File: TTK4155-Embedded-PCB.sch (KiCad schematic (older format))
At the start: 40 parts

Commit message: stated working on pcb
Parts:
- removed J?: AVR-JTAG-10, symbol Connector:AVR-JTAG-10
- removed U?: IDT7164S, Package_DIP:DIP-28_W7.62mm_Socket_LongPads, symbol ByggernCustom:IDT7164S
- added J1: AVR-JTAG-10, Connector_IDC:IDC-Header_2x05_P2.54mm_Vertical, symbol Connector:AVR-JTAG-10
- added U3: IDT7164S, Package_DIP:DIP-28_W7.62mm_Socket_LongPads, symbol ByggernCustom:IDT7164S
- U5: renamed from U?; footprint SN74ALS573CN:DIP254P762X508-20 -> Package_DIP:DIP-20_W7.62mm_Socket_LongPads
- gave numbers to parts that had none: 37
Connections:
- net +5V: now also J1.4 (VREF), J1.7 (VCC), U3.28 (Vcc)
- net A0: now also U3.19 (I/O_7)
- net A1: now also U3.18 (I/O_6)
- net A10: now also U3.21 (A10)
- net A11: now also U3.23 (A11)
- net A2: now also U3.17 (I/O_5)
- net A3: now also U3.16 (I/O_4)
- net A4: now also U3.15 (I/O_3)
- net A5: now also U3.11 (I/O_0)
- net A6: now also U3.12 (I/O_1)
- net A7: now also U3.13 (I/O_2)
- net A8: now also U3.25 (A8)
- net A9: now also U3.24 (A9)
- net CS_RAM: now also U3.26 (CS)
- net GND: now also J1.10 (GND), J1.2 (GND), U3.14 (GND), U3.2 (A12), U3.20 (~CS)
- net TCK: now also J1.1 (TCK)
- net TDI: now also J1.9 (TDI)
- net TDO: now also J1.3 (TDO)
- net TMS: now also J1.5 (TMS)
- net ~OE: now also U3.22 (~OE)
- net ~RESET: now also J1.6 (~SRST)
- net ~WE: now also U3.27 (~WE)
- net at U5.12 (8Q): now also U3.10 (A0)
- net at U5.13 (7Q): now also U3.9 (A1)
- net at U5.14 (6Q): now also U3.8 (A2)
- net at U5.15 (5Q): now also U3.7 (A3)
- net at U5.16 (4Q): now also U3.6 (A4)
- net at U5.17 (3Q): now also U3.5 (A5)
- net at U5.18 (2Q): now also U3.4 (A6)
- net at U5.19 (1Q): now also U3.3 (A7)

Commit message: Started tracing
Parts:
- removed J3: Conn_01x08_Male, Connector_PinHeader_2.00mm:PinHeader_1x08_P2.00mm_Vertical, symbol Connector:Conn_01x08_Male
- removed J5: Conn_01x02_Male, Connector_PinHeader_2.00mm:PinHeader_1x02_P2.00mm_Vertical, symbol Connector:Conn_01x02_Male
- added J3: Conn_01x10_Male, Connector_PinHeader_2.54mm:PinHeader_1x10_P2.54mm_Vertical, symbol Connector:Conn_01x10_Male
- added J5, J6: Screw_Terminal_01x02, TerminalBlock_MetzConnect:TerminalBlock_MetzConnect_Type073_RT02602HBLU_1x02_P5.08mm_Horizontal, symbol Connector:Screw_Terminal_01x02
- added R6: 60R, Resistor_SMD:R_0805_2012Metric_Pad1.15x1.40mm_HandSolder, symbol Device:R
- J4: footprint Connector_PinHeader_2.00mm:PinHeader_1x04_P2.00mm_Vertical -> Connector_PinHeader_2.54mm:PinHeader_1x04_P2.54mm_Vertical
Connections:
- net A0: now also J3.1 (Pin_1)
- net A1: now also J3.2 (Pin_2)
- net A10: now also U3.24 (A9), U4.2 (I2); no longer U3.21 (A10), U4.3 (I3)
- net A11: now also U3.25 (A8), U4.1 (I1/CLK); no longer U3.23 (A11), U4.4 (I4)
- net A2: now also J3.3 (Pin_3)
- net A3: now also J3.4 (Pin_4)
- net A4: now also J3.5 (Pin_5)
- net A5: now also J3.6 (Pin_6)
- net A6: now also J3.7 (Pin_7)
- net A7: now also J3.8 (Pin_8)
- net A8: now also U3.21 (A10); no longer U3.25 (A8), U4.1 (I1/CLK)
- net A9: now also U3.23 (A11), U4.3 (I3); no longer U3.24 (A9), U4.2 (I2)
- net GND: now also J6.2 (Pin_2)
- net OLED_CMD: now also J3.10 (Pin_10)
- net OLED_DATA: now also J3.9 (Pin_9)
- net at U7.6 (CANL): now also J5.2 (Pin_2), R6.2
- net at U7.7 (CANH): now also J5.1 (Pin_1), R6.1
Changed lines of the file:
@@
 Text Label 3350 5300 0    50   ~ 0
 ~OE
-Wire Wire Line
-	4100 3700 4100 3900
-Wire Wire Line
-	4100 3900 4300 3900
-Wire Wire Line
-	4050 3800 4050 4000
-Wire Wire Line
-	4050 4000 4300 4000
-Wire Wire Line
-	4000 4100 4300 4100
-Wire Wire Line
-	3950 4200 4300 4200
-Wire Wire Line
-	3950 4000 3950 4200
 $Comp
 L power:GND #PWR0120
@@
 Wire Wire Line
 	5550 3100 5100 3100
-Wire Wire Line
-	3350 3700 4100 3700
-Wire Wire Line
-	3350 3800 4050 3800
-Wire Wire Line
-	3350 3900 4000 3900
-Wire Wire Line
-	3350 4000 3950 4000
 $Comp
 L Logic_Programmable:GAL16V8 U4
@@
 	1    0    0    -1
 $EndComp
-Wire Wire Line
-	4000 3900 4000 4100
+Text Label 5100 2900 0    50   ~ 0
+A8
+Text Label 5100 3000 0    50   ~ 0
+A9
+Text Label 5100 2800 0    50   ~ 0
+A10
 Text Label 5100 2700 0    50   ~ 0
-A8
-Text Label 5100 2800 0    50   ~ 0
-A9
-Text Label 5100 2900 0    50   ~ 0
-A10
-Text Label 5100 3000 0    50   ~ 0
 A11
 Text Label 3800 3700 0    50   ~ 0
@@
 Reset button
 Wire Notes Line
-	1850 1250 3250 1250
-Wire Notes Line
 	3250 1250 3250 500
 Text Notes 1900 1250 0    50   ~ 0
@@
 Wire Wire Line
 	10050 3200 10000 3200
-Text Label 3650 1900 0    50   ~ 0
-A0
-Text Label 3650 2000 0    50   ~ 0
-A1
-Text Label 3650 2100 0    50   ~ 0
-A2
-Text Label 3650 2200 0    50   ~ 0
-A3
-Text Label 3650 2300 0    50   ~ 0
-A4
-Text Label 3650 2400 0    50   ~ 0
-A5
-Text Label 3650 2500 0    50   ~ 0
-A6
-Text Label 3650 2600 0    50   ~ 0
-A7
 Text Label 10950 2700 0    50   ~ 0
 A0
@@
 F 0 "J4" H 9358 2981 50  0000 C CNN
 F 1 "Conn_01x04_Male" H 9358 2890 50  0000 C CNN
-F 2 "Connector_PinHeader_2.00mm:PinHeader_1x04_P2.00mm_Vertical" H 9250 2700 50  0001 C CNN
+F 2 "Connector_PinHeader_2.54mm:PinHeader_1x04_P2.54mm_Vertical" H 9250 2700 50  0001 C CNN
 F 3 "~" H 9250 2700 50  0001 C CNN
 	1    9250 2700
@@
 Text Notes 10150 3700 0    50   ~ 0
 ADC Converter
-$Comp
-L Connector:Conn_01x08_Male J3
-U 1 1 5DC60D2B
-P 9200 4250
-F 0 "J3" H 9308 4731 50  0000 C CNN
-F 1 "Conn_01x08_Male" H 9308 4640 50  0000 C CNN
-F 2 "Connector_PinHeader_2.00mm:PinHeader_1x08_P2.00mm_Vertical" H 9200 4250 50  0001 C CNN
-F 3 "~" H 9200 4250 50  0001 C CNN
-	1    9200 4250
-	1    0    0    -1
-$EndComp
-Wire Wire Line
-	9400 3950 9600 3950
-Wire Wire Line
-	9400 4050 9600 4050
-Wire Wire Line
-	9400 4150 9600 4150
-Wire Wire Line
-	9400 4250 9600 4250
-Wire Wire Line
-	9400 4350 9600 4350
-Wire Wire Line
-	9400 4450 9600 4450
-Wire Wire Line
-	9400 4550 9600 4550
-Wire Wire Line
-	9400 4650 9600 4650
-Text Label 9600 3950 0    50   ~ 0
+Wire Wire Line
+	9750 3950 9950 3950
+Wire Wire Line
+	9750 4050 9950 4050
+Wire Wire Line
+	9750 4150 9950 4150
+Wire Wire Line
+	9750 4250 9950 4250
+Wire Wire Line
+	9750 4350 9950 4350
+Wire Wire Line
+	9750 4450 9950 4450
+Wire Wire Line
+	9750 4550 9950 4550
+Wire Wire Line
+	9750 4650 9950 4650
+Text Label 9950 3950 0    50   ~ 0
 A0
-Text Label 9600 4050 0    50   ~ 0
+Text Label 9950 4050 0    50   ~ 0
 A1
-Text Label 9600 4150 0    50   ~ 0
+Text Label 9950 4150 0    50   ~ 0
 A2
-Text Label 9600 4250 0    50   ~ 0
+Text Label 9950 4250 0    50   ~ 0
 A3
-Text Label 9600 4350 0    50   ~ 0
+Text Label 9950 4350 0    50   ~ 0
 A4
-Text Label 9600 4450 0    50   ~ 0
+Text Label 9950 4450 0    50   ~ 0
 A5
-Text Label 9600 4550 0    50   ~ 0
+Text Label 9950 4550 0    50   ~ 0
 A6
-Text Label 9600 4650 0    50   ~ 0
+Text Label 9950 4650 0    50   ~ 0
 A7
-Text Notes 9200 4750 0    50   ~ 0
+Text Notes 10150 3950 0    50   ~ 0
 Memory bus to ExtOLED
-$Comp
-L Connector:Conn_01x02_Male J5
-U 1 1 5DCBC334
-P 10450 4050
-F 0 "J5" H 10422 3932 50  0000 R CNN
-F 1 "Conn_01x02_Male" H 10422 4023 50  0000 R CNN
-F 2 "Connector_PinHeader_2.00mm:PinHeader_1x02_P2.00mm_Vertical" H 10450 4050 50  0001 C CNN
-F 3 "~" H 10450 4050 50  0001 C CNN
-	1    10450 4050
-	-1   0    0    1
-$EndComp
 Wire Wire Line
 	5300 4100 5500 4100
@@
 Text Label 5500 4200 0    50   ~ 0
 OLED_DATA
-Text Label 10250 4050 2    50   ~ 0
+Text Label 9750 4850 0    50   ~ 0
 OLED_CMD
-Text Label 10250 3950 2    50   ~ 0
+Text Label 9750 4750 0    50   ~ 0
 OLED_DATA
 Wire Notes Line
-	8950 4800 11200 4800
-Wire Notes Line
-	8950 500  8950 4800
-Text Notes 10000 4250 0    50   ~ 0
+	8950 4950 11200 4950
+Text Notes 10250 4850 0    50   ~ 0
 Selects between data \nand cmd registert\n
 Wire Wire Line
@@
 	1    0    0    -1
 $EndComp
+$Comp
+L Connector:Conn_01x10_Male J3
+U 1 1 5DC3E321
+P 9550 4350
+F 0 "J3" H 9658 4931 50  0000 C CNN
+F 1 "Conn_01x10_Male" H 9658 4840 50  0000 C CNN
+F 2 "Connector_PinHeader_2.54mm:PinHeader_1x10_P2.54mm_Vertical" H 9550 4350 50  0001 C CNN
+F 3 "~" H 9550 4350 50  0001 C CNN
+	1    9550 4350
+	1    0    0    -1
+$EndComp
+Wire Notes Line
+	8950 500  8950 4950
+$Comp
+L Device:R R6
+U 1 1 5DC5E47D
+P 10900 5700
+F 0 "R6" H 10970 5746 50  0000 L CNN
+F 1 "60R" H 10970 5655 50  0000 L CNN
+F 2 "Resistor_SMD:R_0805_2012Metric_Pad1.15x1.40mm_HandSolder" V 10830 5700 50  0001 C CNN
+F 3 "~" H 10900 5700 50  0001 C CNN
+	1    10900 5700
+	1    0    0    -1
+$EndComp
+Wire Wire Line
+	10800 5800 10800 5850
+Wire Wire Line
+	10800 5850 10900 5850
+Wire Wire Line
+	10800 5600 10800 5550
+Wire Wire Line
+	10800 5550 10900 5550
+Wire Wire Line
+	3350 4000 3800 4000
+Wire Wire Line
+	3350 3900 3800 3900
+Wire Wire Line
+	3350 3800 3800 3800
+Wire Wire Line
+	3350 3700 3800 3700
+Text Label 4300 3900 2    50   ~ 0
+A11
+Text Label 4300 4000 2    50   ~ 0
+A10
+Text Label 4300 4100 2    50   ~ 0
+A9
+$Comp
+L Connector:Screw_Terminal_01x02 J5
+U 1 1 5DCCBD1E
+P 11100 6300
+F 0 "J5" V 11100 5950 50  0000 L CNN
+F 1 "Screw_Terminal_01x02" V 11250 5550 50  0000 L CNN
+F 2 "TerminalBlock_MetzConnect:TerminalBlock_MetzConnect_Type073_RT02602HBLU_1x02_P5.08mm_Horizontal" H 11100 6300 50  0001 C CNN
+F 3 "~" H 11100 6300 50  0001 C CNN
+	1    11100 6300
+	0    1    1    0
+$EndComp
+Wire Wire Line
+	10900 5850 11000 5850
+Wire Wire Line
+	11000 5850 11000 6100
+Connection ~ 10900 5850
+Wire Wire Line
+	11100 5850 11150 5850
+Wire Wire Line
+	11150 5850 11150 5550
+Wire Wire Line
+	11150 5550 10900 5550
+Wire Wire Line
+	11100 5850 11100 6100
+Connection ~ 10900 5550
+$Comp
+L Connector:Screw_Terminal_01x02 J6
+U 1 1 5DD11A7E
+P 3550 700
+F 0 "J6" V 3550 350 50  0000 L CNN
+F 1 "Screw_Terminal_01x02" V 3700 100 50  0000 L CNN
+F 2 "TerminalBlock_MetzConnect:TerminalBlock_MetzConnect_Type073_RT02602HBLU_1x02_P5.08mm_Horizontal" H 3550 700 50  0001 C CNN
+F 3 "~" H 3550 700 50  0001 C CNN
+	1    3550 700
+	0    -1   -1   0
+$EndComp
+Wire Wire Line
+	3550 900  3550 1000
+Wire Wire Line
+	3550 1000 3350 1000
+$Comp
+L power:GND #PWR0134
+U 1 1 5DD5A4AB
+P 3650 900
+F 0 "#PWR0134" H 3650 650 50  0001 C CNN
+F 1 "GND" H 3655 727 50  0000 C CNN
+F 2 "" H 3650 900 50  0001 C CNN
+F 3 "" H 3650 900 50  0001 C CNN
+	1    3650 900
+	1    0    0    -1
+$EndComp
+Wire Notes Line
+	3800 1250 3800 950
+Wire Notes Line
+	3800 950  4200 950
+Wire Notes Line
+	4200 950  4200 500
+Wire Notes Line
+	1850 1250 3800 1250
+Text Label 3650 2600 0    50   ~ 0
+A7
+Text Label 3650 2500 0    50   ~ 0
+A6
+Text Label 3650 2400 0    50   ~ 0
+A5
+Text Label 3650 2300 0    50   ~ 0
+A4
+Text Label 3650 2200 0    50   ~ 0
+A3
+Text Label 3650 2100 0    50   ~ 0
+A2
+Text Label 3650 2000 0    50   ~ 0
+A1
+Text Label 3650 1900 0    50   ~ 0
+A0
 $EndSCHEMATC

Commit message: Finished first revision of board
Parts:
- added J7: Conn_01x04_Male, Connector_PinHeader_2.54mm:PinHeader_1x04_P2.54mm_Vertical, symbol Connector:Conn_01x04_Male
- added J8: BannanaJack, TTK4155-Embedded-PCB:Banana_Jack_2Pin_15mm_spacing, symbol Connector_Generic:Conn_01x02
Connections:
- net +12V: now also J6.1 (Pin_1), J8.1 (Pin_1)
- net GND: now also J8.2 (Pin_2)
- net at U2.1 (PB0): now also J7.4 (Pin_4)
- net at U2.2 (PB1): now also J7.3 (Pin_3)
- net at U2.3 (PB2): now also J7.2 (Pin_2)
- net at U2.4 (PB3): now also J7.1 (Pin_1)
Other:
- moved on the sheet: J6
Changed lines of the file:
@@
 L Connector:Screw_Terminal_01x02 J6
 U 1 1 5DD11A7E
-P 3550 700
-F 0 "J6" V 3550 350 50  0000 L CNN
-F 1 "Screw_Terminal_01x02" V 3700 100 50  0000 L CNN
-F 2 "TerminalBlock_MetzConnect:TerminalBlock_MetzConnect_Type073_RT02602HBLU_1x02_P5.08mm_Horizontal" H 3550 700 50  0001 C CNN
-F 3 "~" H 3550 700 50  0001 C CNN
-	1    3550 700
-	0    -1   -1   0
+P 8550 800
+F 0 "J6" V 8650 700 50  0000 L CNN
+F 1 "Screw_Terminal_01x02" V 8750 200 50  0001 L CNN
+F 2 "TerminalBlock_MetzConnect:TerminalBlock_MetzConnect_Type073_RT02602HBLU_1x02_P5.08mm_Horizontal" H 8550 800 50  0001 C CNN
+F 3 "~" H 8550 800 50  0001 C CNN
+	1    8550 800
+	1    0    0    -1
 $EndComp
-Wire Wire Line
-	3550 900  3550 1000
-Wire Wire Line
-	3550 1000 3350 1000
 $Comp
 L power:GND #PWR0134
 U 1 1 5DD5A4AB
-P 3650 900
-F 0 "#PWR0134" H 3650 650 50  0001 C CNN
-F 1 "GND" H 3655 727 50  0000 C CNN
-F 2 "" H 3650 900 50  0001 C CNN
-F 3 "" H 3650 900 50  0001 C CNN
-	1    3650 900
+P 8350 900
+F 0 "#PWR0134" H 8350 650 50  0001 C CNN
+F 1 "GND" H 8355 727 50  0000 C CNN
+F 2 "" H 8350 900 50  0001 C CNN
+F 3 "" H 8350 900 50  0001 C CNN
+	1    8350 900
 	1    0    0    -1
 $EndComp
-Wire Notes Line
-	3800 1250 3800 950
-Wire Notes Line
-	3800 950  4200 950
-Wire Notes Line
-	4200 950  4200 500
-Wire Notes Line
-	1850 1250 3800 1250
 Text Label 3650 2600 0    50   ~ 0
 A7
@@
 Text Label 3650 1900 0    50   ~ 0
 A0
+$Comp
+L power:+12V #PWR0135
+U 1 1 5DDD0920
+P 8350 800
+F 0 "#PWR0135" H 8350 650 50  0001 C CNN
+F 1 "+12V" H 8365 973 50  0000 C CNN
+F 2 "" H 8350 800 50  0001 C CNN
+F 3 "" H 8350 800 50  0001 C CNN
+	1    8350 800
+	1    0    0    -1
+$EndComp
+$Comp
+L Connector:Conn_01x04_Male J7
+U 1 1 5DDF74B0
+P 3550 3000
+F 0 "J7" H 3522 2882 50  0000 R CNN
+F 1 "Conn_01x04_Male" H 3522 2973 50  0000 R CNN
+F 2 "Connector_PinHeader_2.54mm:PinHeader_1x04_P2.54mm_Vertical" H 3550 3000 50  0001 C CNN
+F 3 "~" H 3550 3000 50  0001 C CNN
+	1    3550 3000
+	-1   0    0    1
+$EndComp
+Wire Notes Line
+	3250 1250 1850 1250
+$Comp
+L Connector_Generic:Conn_01x02 J8
+U 1 1 5DE8CCC3
+P 8300 1250
+F 0 "J8" H 8380 1242 50  0000 L CNN
+F 1 "BannanaJack" H 8380 1151 50  0000 L CNN
+F 2 "TTK4155-Embedded-PCB:Banana_Jack_2Pin_15mm_spacing" H 8300 1250 50  0001 C CNN
+F 3 "~" H 8300 1250 50  0001 C CNN
+	1    8300 1250
+	1    0    0    -1
+$EndComp
+$Comp
+L power:GND #PWR0136
+U 1 1 5DE9BBA9
+P 8100 1350
+F 0 "#PWR0136" H 8100 1100 50  0001 C CNN
+F 1 "GND" H 8105 1177 50  0000 C CNN
+F 2 "" H 8100 1350 50  0001 C CNN
+F 3 "" H 8100 1350 50  0001 C CNN
+	1    8100 1350
+	1    0    0    -1
+$EndComp
+$Comp
+L power:+12V #PWR0137
+U 1 1 5DEE3528
+P 8100 1250
+F 0 "#PWR0137" H 8100 1100 50  0001 C CNN
+F 1 "+12V" H 8115 1423 50  0000 C CNN
+F 2 "" H 8100 1250 50  0001 C CNN
+F 3 "" H 8100 1250 50  0001 C CNN
+	1    8100 1250
+	1    0    0    -1
+$EndComp
+Wire Notes Line
+	8950 1650 7900 1650
+Wire Notes Line
+	7900 1650 7900 500
 $EndSCHEMATC

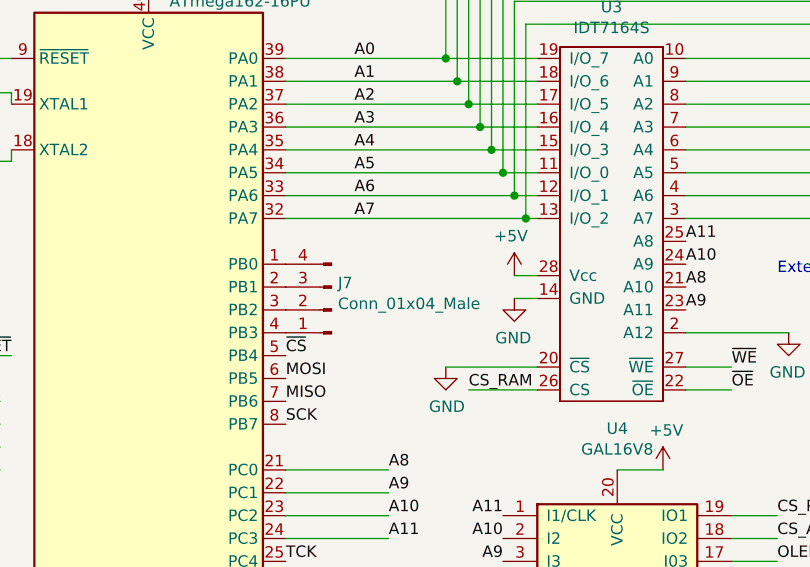
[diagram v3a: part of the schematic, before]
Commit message: Fixed missing pullup
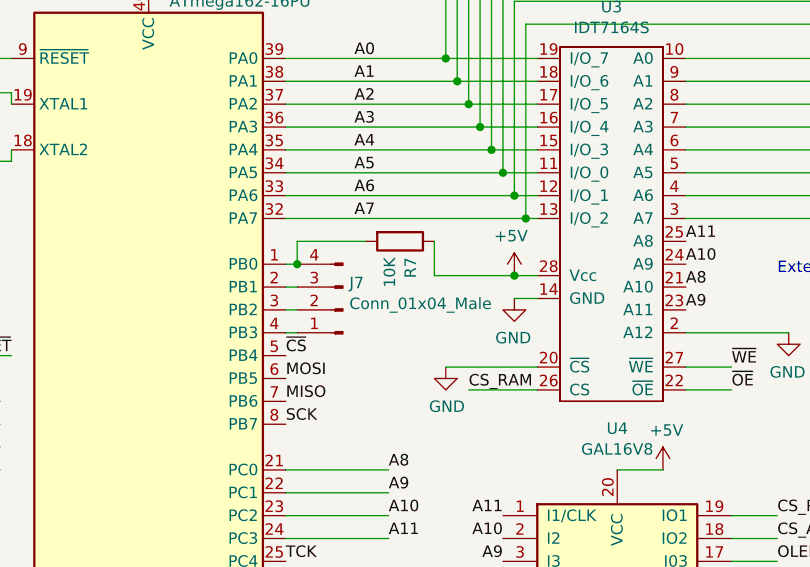
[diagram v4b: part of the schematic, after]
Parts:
- added R7: 10K, Resistor_SMD:R_0805_2012Metric_Pad1.15x1.40mm_HandSolder, symbol Device:R
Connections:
- net +5V: now also R7.1
- net at J7.4 (Pin_4), U2.1 (PB0): now also R7.2
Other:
- moved on the sheet: J7
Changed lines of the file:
@@
 L Connector:Conn_01x04_Male J7
 U 1 1 5DDF74B0
-P 3550 3000
-F 0 "J7" H 3522 2882 50  0000 R CNN
-F 1 "Conn_01x04_Male" H 3522 2973 50  0000 R CNN
-F 2 "Connector_PinHeader_2.54mm:PinHeader_1x04_P2.54mm_Vertical" H 3550 3000 50  0001 C CNN
-F 3 "~" H 3550 3000 50  0001 C CNN
-	1    3550 3000
+P 3600 3000
+F 0 "J7" H 3572 2882 50  0000 R CNN
+F 1 "Conn_01x04_Male" H 3572 2973 50  0000 R CNN
+F 2 "Connector_PinHeader_2.54mm:PinHeader_1x04_P2.54mm_Vertical" H 3600 3000 50  0001 C CNN
+F 3 "~" H 3600 3000 50  0001 C CNN
+	1    3600 3000
 	-1   0    0    1
 $EndComp
@@
 Wire Notes Line
 	7900 1650 7900 500
+$Comp
+L Device:R R7
+U 1 1 5DF418AD
+P 3850 2700
+F 0 "R7" H 3920 2746 50  0000 L CNN
+F 1 "10K" H 3920 2655 50  0000 L CNN
+F 2 "Resistor_SMD:R_0805_2012Metric_Pad1.15x1.40mm_HandSolder" V 3780 2700 50  0001 C CNN
+F 3 "~" H 3850 2700 50  0001 C CNN
+	1    3850 2700
+	0    1    1    0
+$EndComp
+Wire Wire Line
+	3350 2800 3400 2800
+Wire Wire Line
+	3400 2800 3400 2700
+Wire Wire Line
+	3400 2700 3700 2700
+Connection ~ 3400 2800
+Wire Wire Line
+	3350 2900 3400 2900
+Wire Wire Line
+	3350 3000 3400 3000
+Wire Wire Line
+	3350 3100 3400 3100
+Wire Wire Line
+	4000 2700 4000 2850
+Wire Wire Line
+	4000 2850 4350 2850
+Connection ~ 4350 2850
 $EndSCHEMATC

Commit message: Made som esmall changes and send pcb to production
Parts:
- added R10, R8, R9: 10K, Resistor_SMD:R_0805_2012Metric_Pad1.15x1.40mm_HandSolder, symbol Device:R
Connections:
- net +5V: now also R7.2, R10.2, R8.2, R9.2; no longer R7.1
- net PB0: now reaches J7.4 (Pin_4), U2.1 (PB0)
- net PB0: now also R7.1; no longer R7.2
- net PB1: now reaches J7.3 (Pin_3), U2.2 (PB1)
- net PB1: now also R8.1
- net PB2: now reaches J7.2 (Pin_2), U2.3 (PB2)
- net PB2: now also R9.1
- net PB3: now reaches J7.1 (Pin_1), U2.4 (PB3)
- net PB3: now also R10.1
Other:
- moved on the sheet: J7
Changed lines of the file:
@@
 L Connector:Conn_01x04_Male J7
 U 1 1 5DDF74B0
-P 3600 3000
-F 0 "J7" H 3572 2882 50  0000 R CNN
-F 1 "Conn_01x04_Male" H 3572 2973 50  0000 R CNN
-F 2 "Connector_PinHeader_2.54mm:PinHeader_1x04_P2.54mm_Vertical" H 3600 3000 50  0001 C CNN
-F 3 "~" H 3600 3000 50  0001 C CNN
-	1    3600 3000
+P 3700 3000
+F 0 "J7" H 3672 2882 50  0000 R CNN
+F 1 "Conn_01x04_Male" H 3672 2973 50  0001 R CNN
+F 2 "Connector_PinHeader_2.54mm:PinHeader_1x04_P2.54mm_Vertical" H 3700 3000 50  0001 C CNN
+F 3 "~" H 3700 3000 50  0001 C CNN
+	1    3700 3000
 	-1   0    0    1
 $EndComp
@@
 $Comp
 L Device:R R7
-U 1 1 5DF418AD
-P 3850 2700
-F 0 "R7" H 3920 2746 50  0000 L CNN
-F 1 "10K" H 3920 2655 50  0000 L CNN
-F 2 "Resistor_SMD:R_0805_2012Metric_Pad1.15x1.40mm_HandSolder" V 3780 2700 50  0001 C CNN
-F 3 "~" H 3850 2700 50  0001 C CNN
-	1    3850 2700
-	0    1    1    0
+U 1 1 5DB3F4E5
+P 700 6450
+F 0 "R7" H 770 6496 50  0000 L CNN
+F 1 "10K" H 770 6405 50  0000 L CNN
+F 2 "Resistor_SMD:R_0805_2012Metric_Pad1.15x1.40mm_HandSolder" V 630 6450 50  0001 C CNN
+F 3 "~" H 700 6450 50  0001 C CNN
+	1    700  6450
+	-1   0    0    1
+$EndComp
+Text Label 3350 2800 0    50   ~ 0
+PB0
+Text Label 3350 2900 0    50   ~ 0
+PB1
+Text Label 3350 3000 0    50   ~ 0
+PB2
+Text Label 3350 3100 0    50   ~ 0
+PB3
+Wire Wire Line
+	3350 2800 3500 2800
+Wire Wire Line
+	3350 2900 3500 2900
+Wire Wire Line
+	3350 3000 3500 3000
+Wire Wire Line
+	3350 3100 3500 3100
+$Comp
+L Device:R R8
+U 1 1 5DB7ED57
+P 1000 6450
+F 0 "R8" H 1070 6496 50  0000 L CNN
+F 1 "10K" H 1070 6405 50  0000 L CNN
+F 2 "Resistor_SMD:R_0805_2012Metric_Pad1.15x1.40mm_HandSolder" V 930 6450 50  0001 C CNN
+F 3 "~" H 1000 6450 50  0001 C CNN
+	1    1000 6450
+	-1   0    0    1
+$EndComp
+$Comp
+L Device:R R9
+U 1 1 5DB7F993
+P 1300 6450
+F 0 "R9" H 1370 6496 50  0000 L CNN
+F 1 "10K" H 1370 6405 50  0000 L CNN
+F 2 "Resistor_SMD:R_0805_2012Metric_Pad1.15x1.40mm_HandSolder" V 1230 6450 50  0001 C CNN
+F 3 "~" H 1300 6450 50  0001 C CNN
+	1    1300 6450
+	-1   0    0    1
+$EndComp
+$Comp
+L Device:R R10
+U 1 1 5DB7F999
+P 1600 6450
+F 0 "R10" H 1670 6496 50  0000 L CNN
+F 1 "10K" H 1670 6405 50  0000 L CNN
+F 2 "Resistor_SMD:R_0805_2012Metric_Pad1.15x1.40mm_HandSolder" V 1530 6450 50  0001 C CNN
+F 3 "~" H 1600 6450 50  0001 C CNN
+	1    1600 6450
+	-1   0    0    1
+$EndComp
+$Comp
+L power:+5V #PWR0138
+U 1 1 5DB8E098
+P 700 6300
+F 0 "#PWR0138" H 700 6150 50  0001 C CNN
+F 1 "+5V" H 715 6473 50  0000 C CNN
+F 2 "" H 700 6300 50  0001 C CNN
+F 3 "" H 700 6300 50  0001 C CNN
+	1    700  6300
+	1    0    0    -1
 $EndComp
 Wire Wire Line
-	3350 2800 3400 2800
+	1600 6300 1300 6300
+Connection ~ 700  6300
+Connection ~ 1000 6300
 Wire Wire Line
-	3400 2800 3400 2700
+	1000 6300 700  6300
+Connection ~ 1300 6300
 Wire Wire Line
-	3400 2700 3700 2700
-Connection ~ 3400 2800
-Wire Wire Line
-	3350 2900 3400 2900
-Wire Wire Line
-	3350 3000 3400 3000
-Wire Wire Line
-	3350 3100 3400 3100
-Wire Wire Line
-	4000 2700 4000 2850
-Wire Wire Line
-	4000 2850 4350 2850
-Connection ~ 4350 2850
+	1300 6300 1000 6300
+Text Label 700  6600 3    50   ~ 0
+PB0
+Text Label 1000 6600 3    50   ~ 0
+PB1
+Text Label 1300 6600 3    50   ~ 0
+PB2
+Text Label 1600 6600 3    50   ~ 0
+PB3
 $EndSCHEMATC
